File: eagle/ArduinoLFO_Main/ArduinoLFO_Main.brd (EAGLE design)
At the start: 70.8 x 45.7 mm, 23 parts, among them IC1 MCP4922

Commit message: Board Design
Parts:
- removed JP3: OUTB, pinhead:1X02
- removed JP4: VREFB, pinhead:1X03
- C1: device rcl:SANYO-OSCON_C6 -> rcl:E2,5-7
- R1, R2, R3, R4: device rcl:0207/7 -> rcl:0204V
- moved R5 60.3 mm to (57.1, 25.4), turned to 180 degrees
- moved JP11 7.62 mm to (6.35, 7.62)
- moved IC1 5.68 mm to (14.0, 26.7)
- moved JP1 5.68 mm to (6.35, 20.3)
- moved JP2 5.68 mm to (5.08, 22.9)
- moved LED3 3.59 mm to (50.8, 41.9)
- moved JP10 3.59 mm to (55.9, 7.62)
- moved JP9 3.59 mm to (45.7, 7.62)
- moved C1 3.59 mm to (17.8, 8.89)
- moved JP5 3.59 mm to (53.3, 31.8)
- moved JP6 3.59 mm to (55.9, 31.8)
- moved LED1 3.59 mm to (35.6, 41.9)
- moved LED2 3.59 mm to (43.2, 41.9)
- moved LED4 3.59 mm to (58.4, 41.9)
- moved U$1 3.59 mm to (57.1, 22.9)
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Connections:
- removed net N$4: IC1.8, U$1.D9
- removed net N$8: IC1.11, JP3.1
- removed net N$9: IC1.10, JP4.1
- net +3V3: no longer JP4.3
- net GND: now also IC1.11; no longer JP3.2, JP4.2

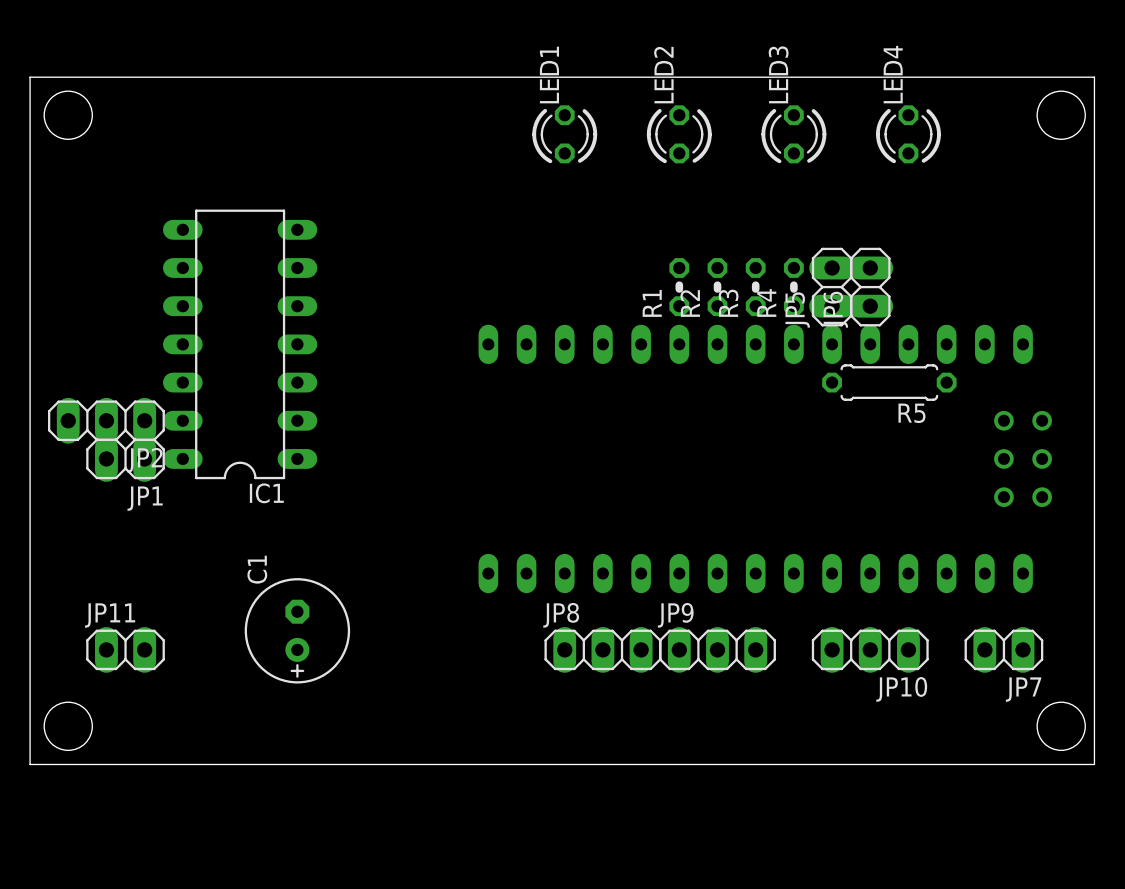
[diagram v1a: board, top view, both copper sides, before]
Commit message: Main Boardはんだ付け完了
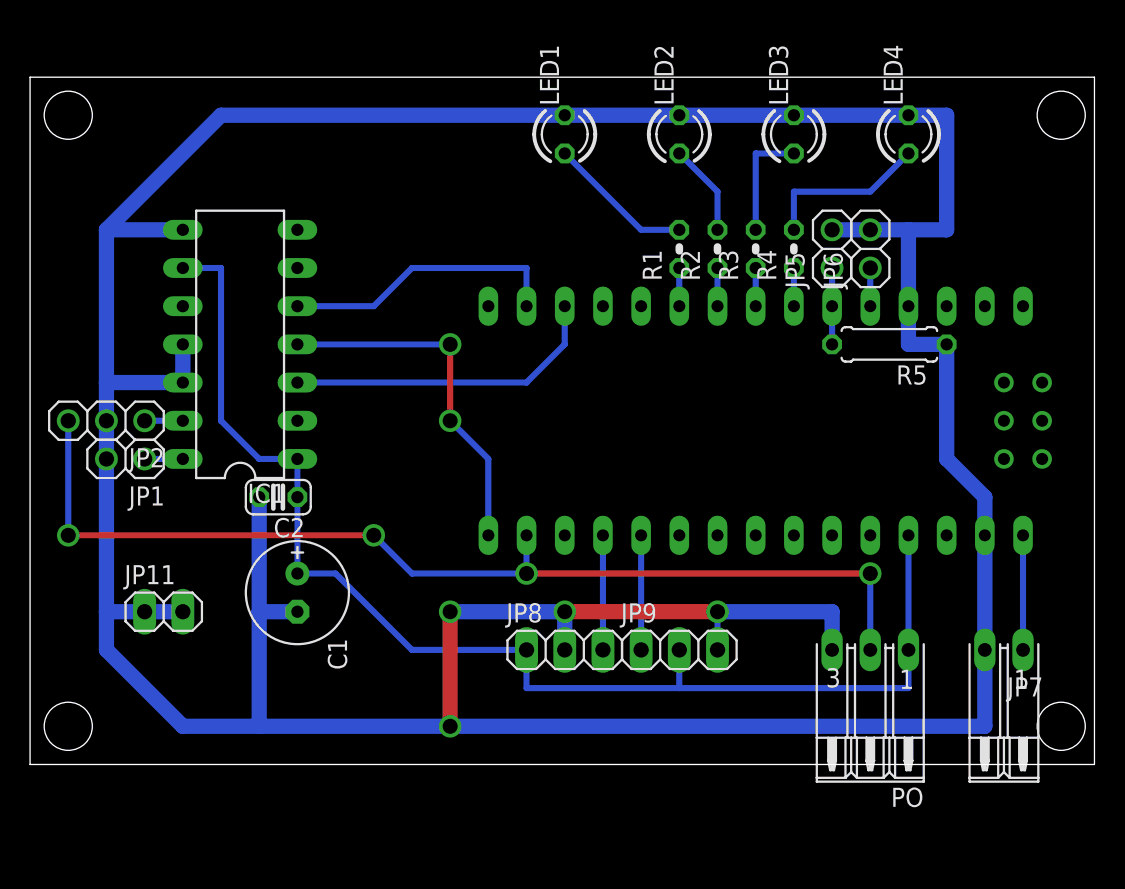
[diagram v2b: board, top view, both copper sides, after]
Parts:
- removed JP10: PWR_OUT, pinhead:1X03
- added C2: 0.1uF, rcl:C025-024X044
- added PO: PWR_OUT, con-amp-quick:03PA
- JP1, JP5: device pinhead:1X02 -> my_pinhead:1X02
- JP2: device pinhead:1X03 -> my_pinhead:1X03
- JP6: value WaveShape -> WavShpe; device pinhead:1X02 -> my_pinhead:1X02
- JP7: device pinhead:1X02 -> con-amp-quick:02PA
- LED1: value GREEN -> LED1
- LED2: value GREEN -> LED2
- LED3: value GREEN -> LED3
- LED4: value GREEN -> LED4
- moved JP11 3.59 mm to (8.89, 10.2)
- moved R5 2.54 mm to (57.1, 27.9)
- moved C1 2.54 mm to (17.8, 11.4), turned to 270 degrees
- moved JP5 2.54 mm to (53.3, 34.3)
- moved JP6 2.54 mm to (55.9, 34.3)
- moved JP8 2.54 mm to (35.6, 7.62)
- moved JP9 2.54 mm to (43.2, 7.62)
- moved R1 2.54 mm to (43.2, 34.3)
- moved R2 2.54 mm to (45.7, 34.3)
- moved R3 2.54 mm to (48.3, 34.3)
- moved R4 2.54 mm to (50.8, 34.3)
- moved U$1 2.54 mm to (57.1, 25.4)
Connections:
- removed net N$5: JP8.2, U$1.A0
- new net N$4: JP8.3, U$1.A0
- net +3V3: now also PO.2; no longer JP10.2
- net +5V: now also C2.1, JP9.2, PO.1; no longer JP10.1, JP9.1
- net GND: now also C2.2, IC1.8, JP8.2, PO.3; no longer JP10.3, JP8.3
- net N$10: now also JP9.1; no longer JP9.2
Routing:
- net GND: track 0.00 -> 275.6 mm, vias 0 -> 4
- net +5V: track 0.00 -> 84.4 mm
- net +3V3: track 0.00 -> 69.6 mm, vias 0 -> 4
- net N$1: track 0.00 -> 23.9 mm, vias 0 -> 2
- net N$3: track 0.00 -> 21.4 mm
- net N$2: track 0.00 -> 18.8 mm
- net N$18: track 0.00 -> 11.2 mm
- net N$15: track 0.00 -> 9.72 mm
- net N$4: track 0.00 -> 7.62 mm
- net N$11: track 0.00 -> 7.62 mm
- net N$10: track 0.00 -> 7.62 mm
- net N$17: track 0.00 -> 7.62 mm
- net N$16: track 0.00 -> 6.13 mm
- net N$23: track 0.00 -> 5.08 mm
- net N$24: track 0.00 -> 2.54 mm
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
